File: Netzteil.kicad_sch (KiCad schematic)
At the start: 11 parts, among them J1 Conn_01x02_Socket, J2 Conn_01x02_Socket, P1 P-trim, U1 LM2596S-ADJ

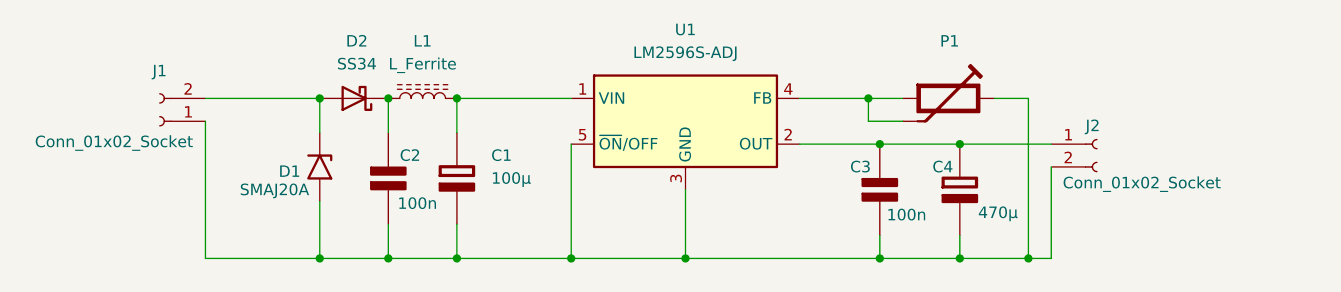
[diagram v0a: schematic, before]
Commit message: Added Footprints.
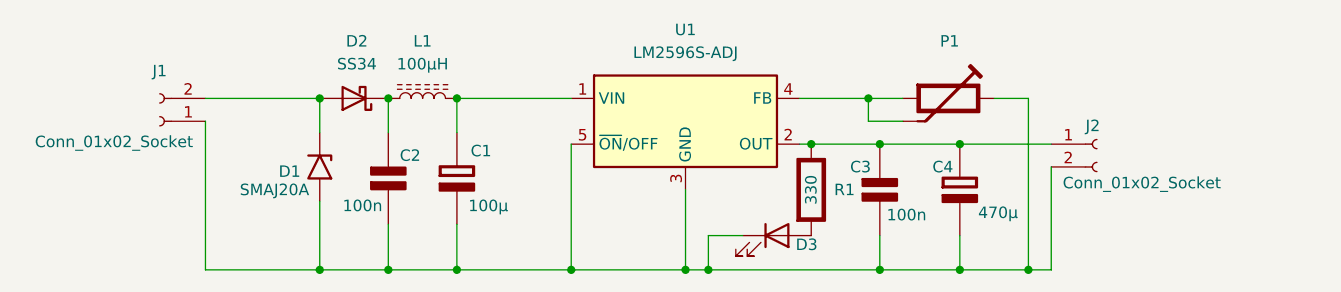
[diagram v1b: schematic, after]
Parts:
- added D3: LED, LED_SMD:LED_Kingbright_AAA3528ESGCT, symbol Device:LED
- added R1: 330, Resistor_SMD:R_MiniMELF_MMA-0204, symbol Elektuur:R
- C1, C4: footprint (none) -> Capacitor_Tantalum_SMD:CP_EIA-3528-12_Kemet-T
- C2, C3: footprint (none) -> Capacitor_SMD:C_0603_1608Metric
- J1, J2: footprint (none) -> TerminalBlock_Phoenix:TerminalBlock_Phoenix_MPT-0,5-2-2.54_1x02_P2.54mm_Horizontal
- L1: value L_Ferrite -> 100µH; footprint (none) -> Inductor_THT:L_Radial_D7.5mm_P5.00mm_Fastron_07P
- P1: footprint (none) -> Potentiometer_THT:Potentiometer_Bourns_3386P_Vertical
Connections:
- net at C3.1 (+), C4.1 (+), J2.1 (Pin_1)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: now also R1.1 (+)
- net at C1.2 (-), C2.2 (-), C3.2 (-)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: now also D3.1 (K)
- new net: D3.2 (A), R1.2 (-)

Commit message: Added Footprints.
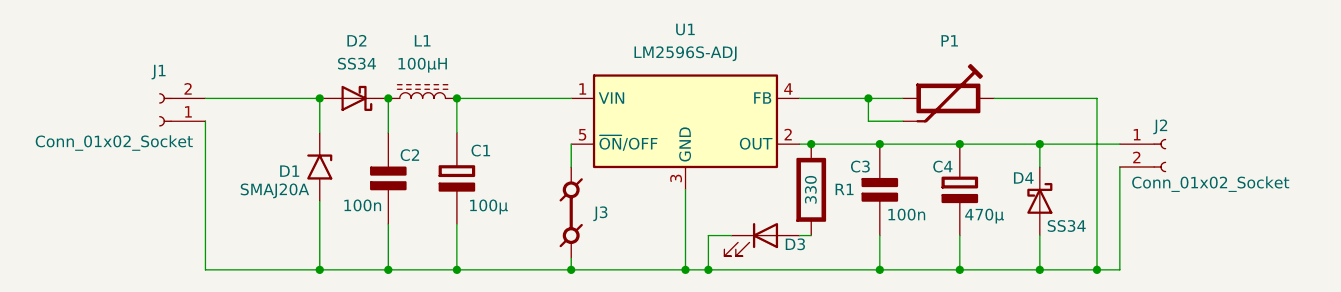
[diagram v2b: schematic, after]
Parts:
- added D4: SS34, Diode_SMD:D_SMA, symbol Diode:SS34
- added J3: J-jumper, Connector_PinHeader_2.54mm:PinHeader_1x02_P2.54mm_Vertical, symbol Elektuur:J-jumper
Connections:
- net at C3.1 (+), C4.1 (+), J2.1 (Pin_1)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: now also D4.1 (K)
- net at C1.2 (-), C2.2 (-), C3.2 (-)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: now also D4.2 (A), J3.2; no longer U1.5 (~{ON}/OFF)
- new net: J3.1, U1.5 (~{ON}/OFF)
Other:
- moved on the sheet: D3, J2
